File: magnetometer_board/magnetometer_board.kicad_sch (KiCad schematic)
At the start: 12 parts, among them J2 S4B-PH-K-S_LF__SN_, U1 MLX90393SLW-ABA-011-RE, U2 MLX90393SLW-ABA-011-RE, U3 MLX90393SLW-ABA-011-RE

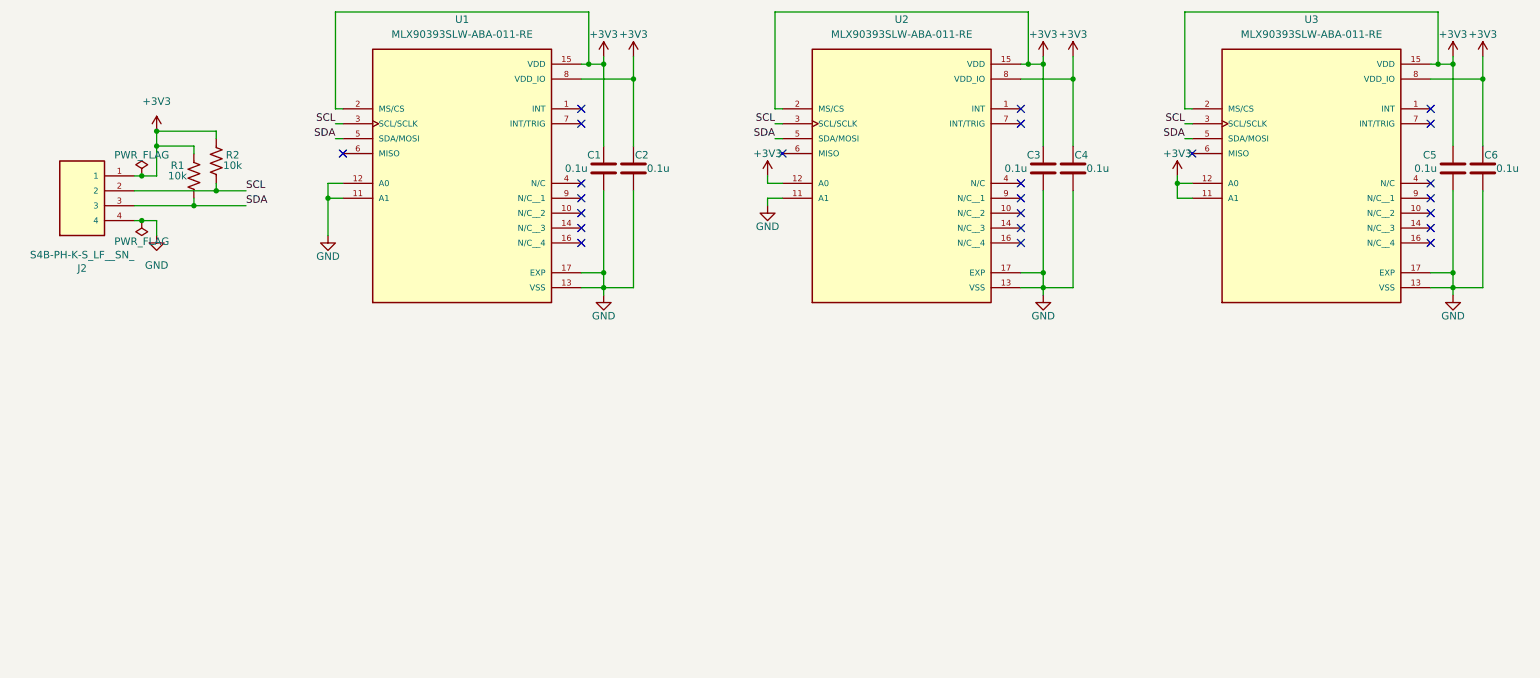
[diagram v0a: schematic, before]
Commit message: Fixed actuator board and revised magnetometer board
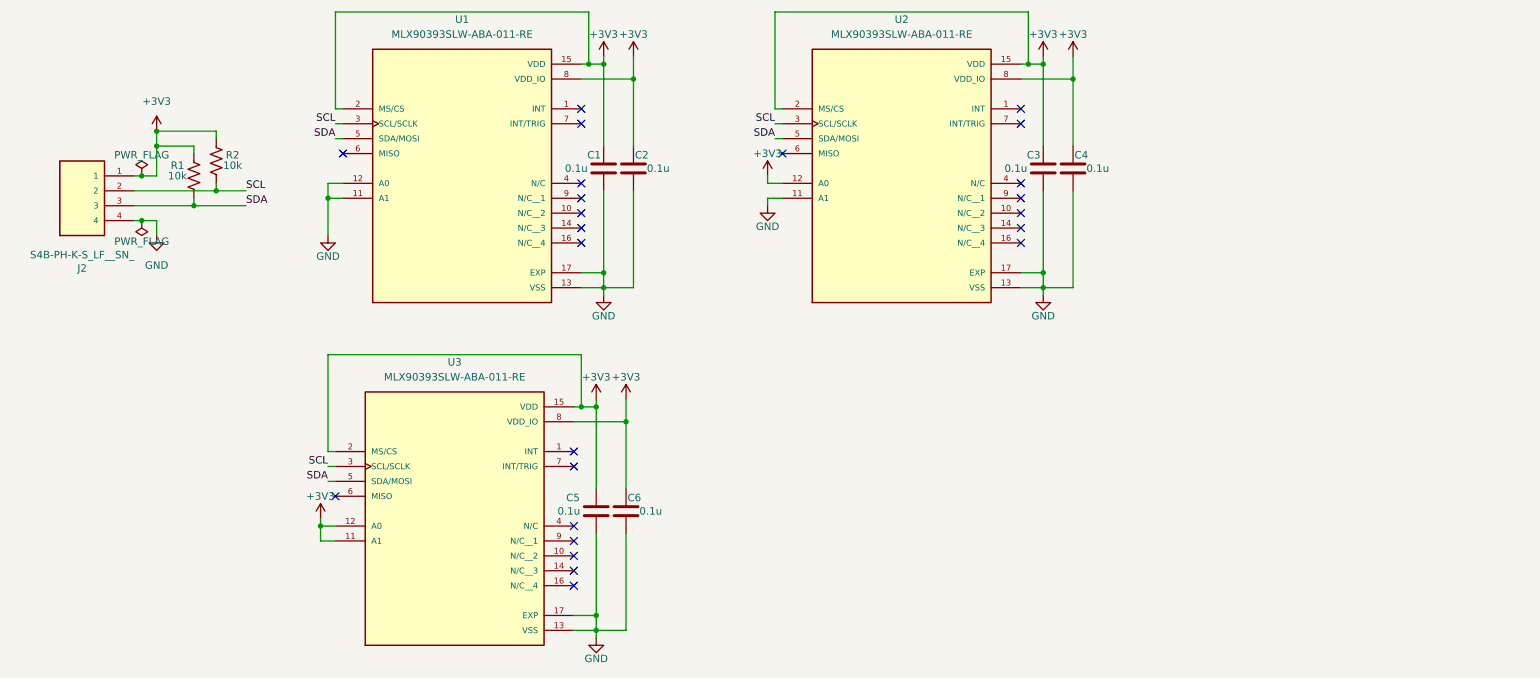
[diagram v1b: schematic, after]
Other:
- moved on the sheet: C5, C6, U3

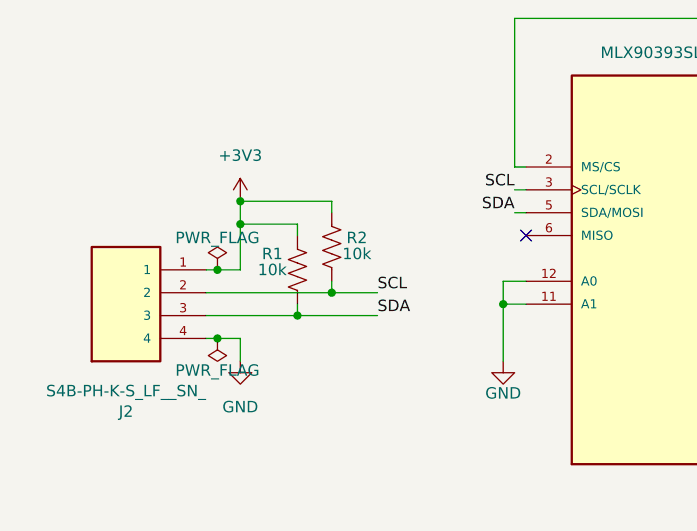
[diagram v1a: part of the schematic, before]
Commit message: Fixed battery issues, removed LDOs
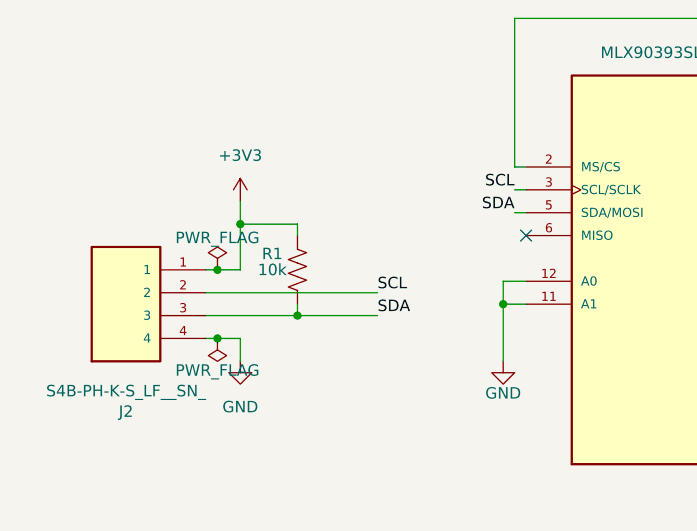
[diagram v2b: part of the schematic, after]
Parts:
- removed R2: 10k, Resistor_SMD:R_0603_1608Metric, symbol Device:R_US
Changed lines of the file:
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@@
-	)
-	(junction
-		(at 53.34 64.77)
-		(diameter 0)
-		(color 0 0 0 0)
 	)
 	(junction
@@
 	)
 	(junction
-		(at 43.18 54.61)
-		(diameter 0)
-		(color 0 0 0 0)
-	)
-	(junction
 		(at 115.57 101.6)
 		(diameter 0)
@@
 	(wire
 		(pts
-			(xy 43.18 54.61) (xy 53.34 54.61)
-		)
-		(stroke
-			(width 0)
-			(type default)
-		)
-	)
-	(wire
-		(pts
 			(xy 49.53 67.31) (xy 58.42 67.31)
 		)
@@
 	(wire
 		(pts
-			(xy 39.37 64.77) (xy 53.34 64.77)
+			(xy 39.37 64.77) (xy 58.42 64.77)
 		)
 		(stroke
@@
 	(wire
 		(pts
-			(xy 53.34 63.5) (xy 53.34 64.77)
-		)
-		(stroke
-			(width 0)
-			(type default)
-		)
-	)
-	(wire
-		(pts
 			(xy 119.38 64.77) (xy 119.38 78.74)
 		)
@@
 	(wire
 		(pts
-			(xy 53.34 54.61) (xy 53.34 55.88)
-		)
-		(stroke
-			(width 0)
-			(type default)
-		)
-	)
-	(wire
-		(pts
 			(xy 148.59 34.29) (xy 191.77 34.29)
 		)
@@
 		(pts
 			(xy 118.11 101.6) (xy 118.11 115.57)
-		)
-		(stroke
-			(width 0)
-			(type default)
-		)
-	)
-	(wire
-		(pts
-			(xy 53.34 64.77) (xy 58.42 64.77)
 		)
 		(stroke
@@
 					(unit 1)
 				)
-			)
-		)
-	)
-	(symbol
-		(lib_id "Device:R_US")
-		(at 53.34 59.69 0)
-		(unit 1)
-		(exclude_from_sim no)
-		(in_bom yes)
-		(on_board yes)
-		(dnp no)
-		(property "Reference" "R2"
-			(at 56.134 58.674 0)
-			(effects
-				(font
-					(size 1.27 1.27)
-				)
-			)
-		)
-		(property "Value" "10k"
-			(at 56.134 60.452 0)
-			(effects
-				(font
-					(size 1.27 1.27)
-				)
-			)
-		)
-		(property "Footprint" "Resistor_SMD:R_0603_1608Metric"
-			(at 54.356 59.944 90)
-			(effects
-				(font
-					(size 1.27 1.27)
-				)
-				(hide yes)
-			)
-		)
-		(property "Datasheet" "~"
-			(at 53.34 59.69 0)
-			(effects
-				(font
-					(size 1.27 1.27)
-				)
-				(hide yes)
-			)
-		)
-		(property "Description" "Resistor, US symbol"
-			(at 53.34 59.69 0)
-			(effects
-				(font
-					(size 1.27 1.27)
-				)
-				(hide yes)
-			)
-		)
-		(pin "1"
-		)
-		(pin "2"
-		)
-		(instances
-			(project "magnetometer_board"
-				(path "/030111b9-3866-4619-8384-eef4a0d75538"
-					(reference "R2")
-					(unit 1)
-				)
